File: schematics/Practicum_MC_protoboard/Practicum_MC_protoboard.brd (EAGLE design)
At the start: 87.1 x 92.1 mm, 49 parts

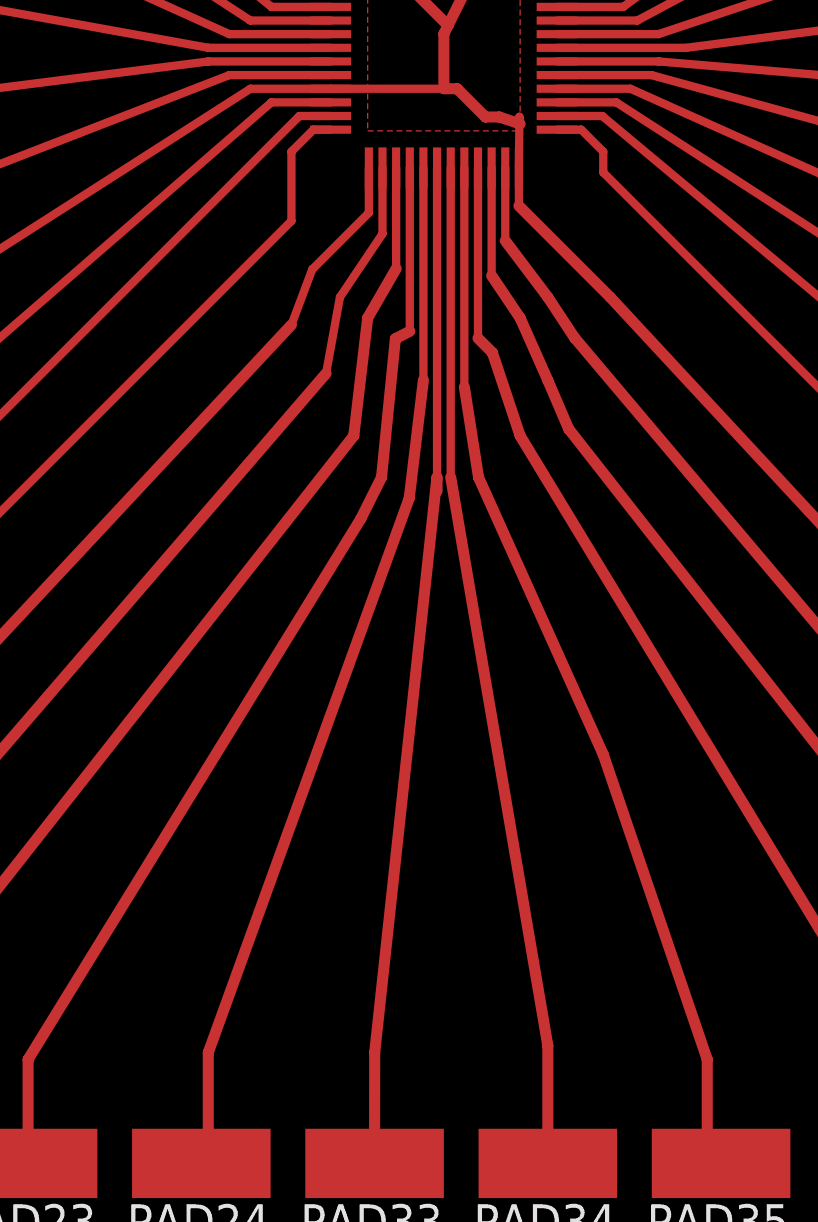
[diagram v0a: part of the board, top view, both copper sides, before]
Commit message: modified dev board layout slightly
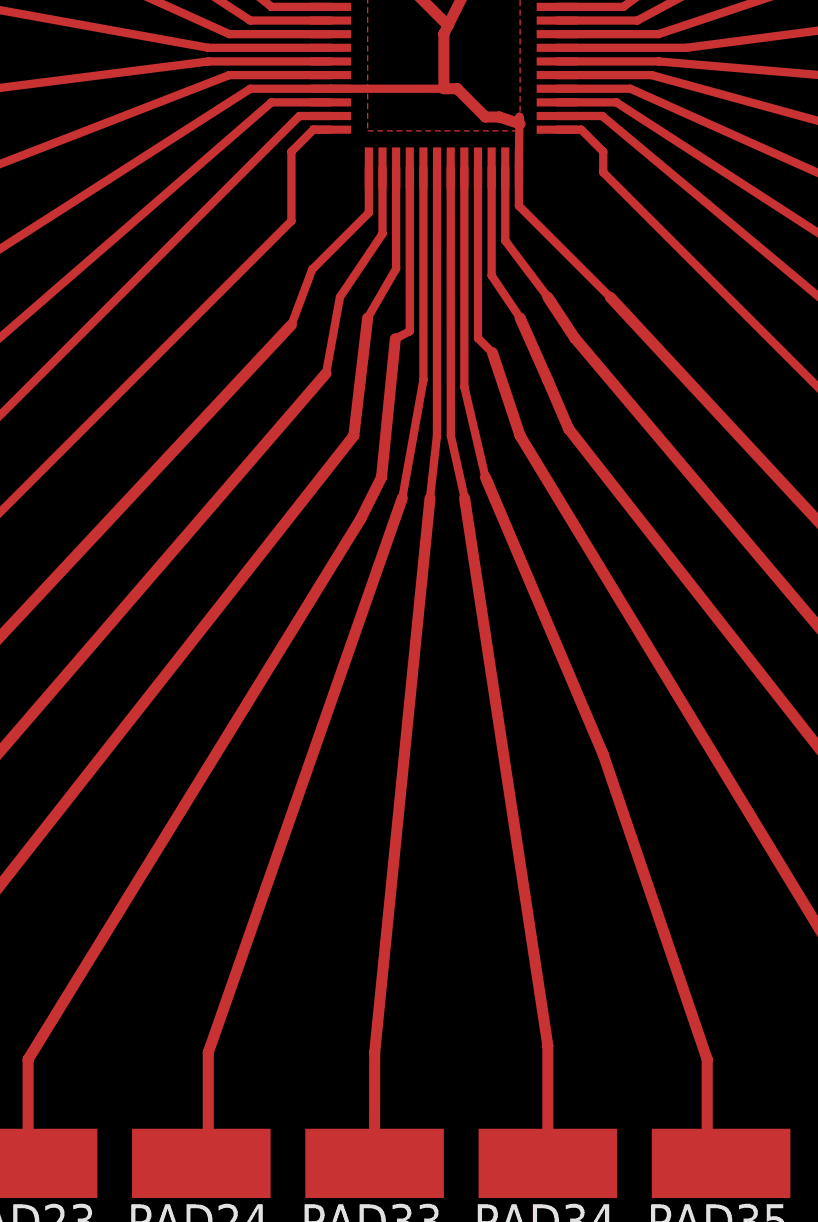
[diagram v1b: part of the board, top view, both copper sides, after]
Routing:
- net N$1: track 37.6 -> 36.6 mm
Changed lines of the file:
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@@
 <contactref element="PAD33" pad="1"/>
 <wire x1="68.58" y1="13.97" x2="68.584" y2="18.038" width="0.4064" layer="1"/>
-<wire x1="68.584" y1="18.038" x2="70.866" y2="39.116" width="0.4064" layer="1"/>
-<wire x1="70.866" y1="39.116" x2="70.87" y2="38.612" width="0.4064" layer="1"/>
-<wire x1="70.87" y1="38.612" x2="70.87" y2="50.46" width="0.3048" layer="1"/>
+<wire x1="68.584" y1="18.038" x2="70.612" y2="38.354" width="0.4064" layer="1"/>
+<wire x1="70.612" y1="38.354" x2="70.616" y2="38.358" width="0.254" layer="1"/>
+<wire x1="70.616" y1="38.358" x2="70.612" y2="38.362" width="0.3048" layer="1"/>
+<wire x1="70.612" y1="38.362" x2="70.866" y2="40.64" width="0.3048" layer="1"/>
+<wire x1="70.866" y1="40.64" x2="70.87" y2="50.46" width="0.3048" layer="1"/>
 </signal>
 <signal name="N$2">
@@
 <contactref element="PAD34" pad="1"/>
 <wire x1="74.93" y1="13.97" x2="74.93" y2="18.288" width="0.4064" layer="1"/>
-<wire x1="74.93" y1="18.288" x2="71.37" y2="39.12" width="0.4064" layer="1"/>
-<wire x1="71.37" y1="39.12" x2="71.37" y2="50.46" width="0.3048" layer="1"/>
+<wire x1="74.93" y1="18.288" x2="71.878" y2="38.358" width="0.4064" layer="1"/>
+<wire x1="71.878" y1="38.358" x2="71.882" y2="38.362" width="0.3048" layer="1"/>
+<wire x1="71.882" y1="38.362" x2="71.374" y2="40.64" width="0.3048" layer="1"/>
+<wire x1="71.374" y1="40.64" x2="71.37" y2="50.46" width="0.3048" layer="1"/>
 </signal>
 <signal name="N$3">
@@
 <wire x1="80.772" y1="14.478" x2="80.772" y2="17.78" width="0.4064" layer="1"/>
 <wire x1="80.772" y1="17.78" x2="76.962" y2="28.956" width="0.4064" layer="1"/>
-<wire x1="76.962" y1="28.956" x2="72.39" y2="39.116" width="0.4064" layer="1"/>
-<wire x1="72.39" y1="39.116" x2="71.87" y2="42.43" width="0.4064" layer="1"/>
+<wire x1="76.962" y1="28.956" x2="72.644" y2="39.116" width="0.4064" layer="1"/>
+<wire x1="72.644" y1="39.116" x2="71.87" y2="42.43" width="0.3048" layer="1"/>
 <wire x1="71.87" y1="42.43" x2="71.87" y2="50.46" width="0.3048" layer="1"/>
 </signal>
@@
 <wire x1="87.63" y1="18.034" x2="73.914" y2="40.64" width="0.4064" layer="1"/>
 <wire x1="73.914" y1="40.64" x2="72.898" y2="43.688" width="0.4064" layer="1"/>
-<wire x1="72.898" y1="43.688" x2="72.37" y2="44.216" width="0.4064" layer="1"/>
+<wire x1="72.898" y1="43.688" x2="72.37" y2="44.216" width="0.3048" layer="1"/>
 <wire x1="72.37" y1="44.216" x2="72.37" y2="50.46" width="0.3048" layer="1"/>
 </signal>
@@
 <wire x1="75.692" y1="40.894" x2="74.93" y2="42.672" width="0.4064" layer="1"/>
 <wire x1="74.93" y1="42.672" x2="73.914" y2="44.958" width="0.4064" layer="1"/>
-<wire x1="73.914" y1="44.958" x2="72.87" y2="46.51" width="0.4064" layer="1"/>
+<wire x1="73.914" y1="44.958" x2="72.87" y2="46.51" width="0.3048" layer="1"/>
 <wire x1="72.87" y1="46.51" x2="72.87" y2="50.46" width="0.3048" layer="1"/>
 </signal>
@@
 <wire x1="62.23" y1="13.97" x2="62.484" y2="14.224" width="0.4064" layer="1"/>
 <wire x1="62.484" y1="14.224" x2="62.484" y2="18.034" width="0.4064" layer="1"/>
-<wire x1="62.484" y1="18.034" x2="69.85" y2="38.354" width="0.4064" layer="1"/>
-<wire x1="69.85" y1="38.354" x2="70.37" y2="42.684" width="0.4064" layer="1"/>
+<wire x1="62.484" y1="18.034" x2="69.596" y2="38.354" width="0.4064" layer="1"/>
+<wire x1="69.596" y1="38.354" x2="70.37" y2="42.684" width="0.3048" layer="1"/>
 <wire x1="70.37" y1="42.684" x2="70.37" y2="50.46" width="0.3048" layer="1"/>
 </signal>
@@
 <wire x1="68.072" y1="37.592" x2="68.834" y2="39.116" width="0.4064" layer="1"/>
 <wire x1="68.834" y1="39.116" x2="69.342" y2="44.196" width="0.4064" layer="1"/>
-<wire x1="69.342" y1="44.196" x2="69.87" y2="44.47" width="0.4064" layer="1"/>
+<wire x1="69.342" y1="44.196" x2="69.87" y2="44.47" width="0.3048" layer="1"/>
 <wire x1="69.87" y1="44.47" x2="69.87" y2="50.46" width="0.3048" layer="1"/>
 </signal>
@@
 <wire x1="50.038" y1="18.034" x2="67.818" y2="40.64" width="0.4064" layer="1"/>
 <wire x1="67.818" y1="40.64" x2="68.326" y2="44.958" width="0.4064" layer="1"/>
-<wire x1="68.326" y1="44.958" x2="69.37" y2="46.764" width="0.4064" layer="1"/>
+<wire x1="68.326" y1="44.958" x2="69.37" y2="46.764" width="0.3048" layer="1"/>
 <wire x1="69.37" y1="46.764" x2="69.37" y2="50.46" width="0.3048" layer="1"/>
 </signal>
@@
 <wire x1="96.52" y1="19.812" x2="75.91" y2="44.232" width="0.4064" layer="1"/>
 <wire x1="75.91" y1="44.232" x2="74.93" y2="45.72" width="0.4064" layer="1"/>
-<wire x1="74.93" y1="45.72" x2="73.37" y2="47.788" width="0.4064" layer="1"/>
+<wire x1="74.93" y1="45.72" x2="73.37" y2="47.788" width="0.3048" layer="1"/>
 <wire x1="73.37" y1="47.788" x2="73.37" y2="50.46" width="0.3048" layer="1"/>
 <wire x1="110.49" y1="83.82" x2="110.236" y2="83.566" width="0.4064" layer="1"/>
@@
 <contactref element="U$1" pad="24"/>
 <wire x1="106.68" y1="13.97" x2="77.216" y2="45.72" width="0.4064" layer="1"/>
-<wire x1="77.216" y1="45.72" x2="73.87" y2="49.066" width="0.4064" layer="1"/>
+<wire x1="77.216" y1="45.72" x2="73.87" y2="49.066" width="0.3048" layer="1"/>
 <wire x1="73.87" y1="50.46" x2="73.87" y2="49.066" width="0.3048" layer="1"/>
 <contactref element="U$1" pad="48"/>
